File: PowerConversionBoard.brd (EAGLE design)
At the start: 152.4 x 101.6 mm, 48 parts, among them U1 LM2678, U2 LM2678

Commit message: Final touch
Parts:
- renumbered J4 to +5V_3.3V, U$8 to 5V_3.3V
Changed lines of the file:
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@@
 <attribute name="VALUE" x="143.7132" y="77.6986" size="0.6096" layer="27" font="vector" ratio="20"/>
 </element>
-<element name="J4" library="SparkFun-Connectors" library_urn="urn:adsk.eagle:library:513" package="BANANA_CONN" package3d_urn="urn:adsk.eagle:package:38018/1" value="" x="96.012" y="96.012" smashed="yes">
-<attribute name="NAME" x="93.472" y="99.314" size="0.6096" layer="25" font="vector" ratio="20"/>
+<element name="+5V_3.3V" library="SparkFun-Connectors" library_urn="urn:adsk.eagle:library:513" package="BANANA_CONN" package3d_urn="urn:adsk.eagle:package:38018/1" value="" x="96.012" y="96.012" smashed="yes">
+<attribute name="NAME" x="93.98" y="92.075" size="0.6096" layer="25" font="vector" ratio="20"/>
 <attribute name="VALUE" x="93.472" y="92.075" size="0.6096" layer="27" font="vector" ratio="20"/>
 </element>
@@
 <attribute name="NAME" x="137.5664" y="92.71" size="0.6096" layer="25"/>
 </element>
-<element name="U$8" library="TP" package="TP" value="TP" x="103.0224" y="96.393" smashed="yes">
-<attribute name="NAME" x="100.7618" y="91.3384" size="1.778" layer="25"/>
+<element name="5V_3.3V" library="TP" package="TP" value="TP" x="103.0224" y="96.393" smashed="yes">
+<attribute name="NAME" x="100.7618" y="92.8624" size="0.6096" layer="25"/>
 </element>
 <element name="U$12" library="ET60S-02-24-02-X-VP-GP" package="ET60S-02-24-02-X-VP-GP" value="ET60S-02-24-02-X-VP-GP" x="76.2" y="12.7" smashed="yes">
@@
 <contactref element="U$4" pad="P$2"/>
 <contactref element="R1" pad="2"/>
-<contactref element="J4" pad="P$1"/>
+<contactref element="+5V_3.3V" pad="P$1"/>
 <wire x1="77.6986" y1="83.5856" x2="71.3486" y2="83.5856" width="1.27" layer="1"/>
 <wire x1="84.0486" y1="83.5856" x2="77.6986" y2="83.5856" width="1.27" layer="1"/>
 <wire x1="84.0486" y1="91.5416" x2="84.0486" y2="83.5856" width="1.27" layer="1"/>
 <contactref element="U$7" pad="2"/>
-<contactref element="U$8" pad="P$1"/>
+<contactref element="5V_3.3V" pad="P$1"/>
 <wire x1="84.0486" y1="91.5416" x2="83.1986" y2="91.5416" width="1.27" layer="1"/>
 <wire x1="71.3486" y1="83.5856" x2="67.773" y2="80.01" width="1.016" layer="1"/>

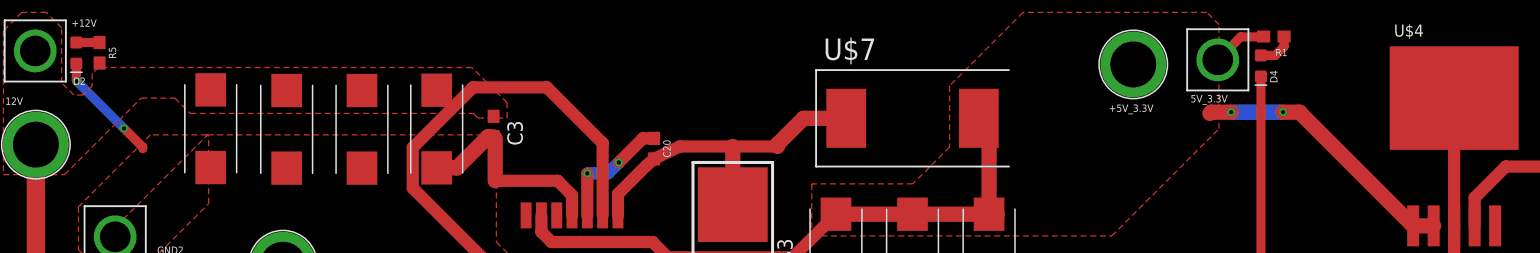
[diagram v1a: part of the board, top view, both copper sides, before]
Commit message: fixed the forward/backward annotation error
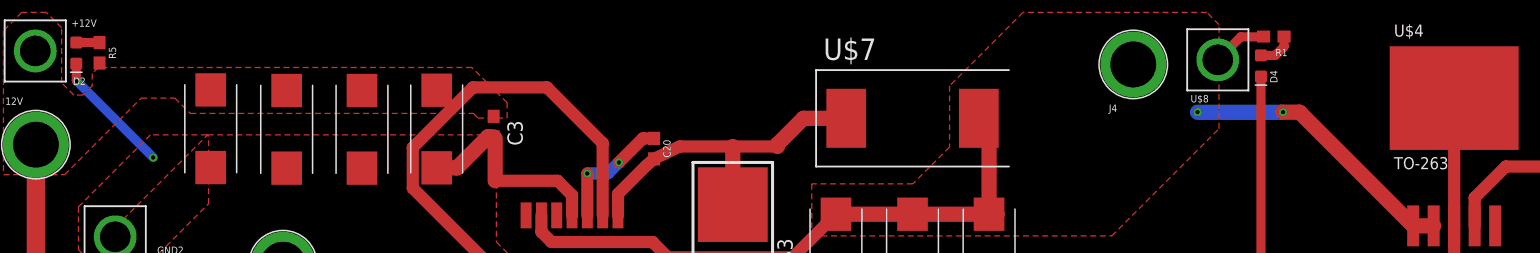
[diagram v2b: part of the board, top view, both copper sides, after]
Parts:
- renumbered +5V_3.3V to J4, 5V_3.3V to U$8
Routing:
- net GND: track 260.8 -> 261.9 mm
- net +5V_3.3V: track 77.5 -> 78.4 mm

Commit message: fixed weird
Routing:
- net +12V: track 138.4 -> 113.5 mm, vias 3 -> 2

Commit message: Board presentation file
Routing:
- net +12V: track 113.5 -> 67.4 mm, vias 2 -> 0
- net GND: track 261.9 -> 261.1 mm, vias 4 -> 5
- removed copper zone on layer 16, net +12V
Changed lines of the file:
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@@
 <?xml version="1.0" encoding="utf-8"?>
 <!DOCTYPE eagle SYSTEM "eagle.dtd">
-<eagle version="9.5.1">
+<eagle version="9.5.0">
 <drawing>
 <settings>
@@
 </class>
 </classes>
-<designrules name="ECE_Senior_Design">
+<designrules name="ECE_Senior_Design (1)">
 <description language="de">&lt;b&gt;EAGLE Design Rules&lt;/b&gt;
 &lt;p&gt;
@@
 <contactref element="U$9" pad="8"/>
 <contactref element="U$9" pad="10"/>
-<polygon width="0.254" layer="1">
-<vertex x="2.286" y="86.868"/>
-<vertex x="7.366" y="86.868"/>
-<vertex x="13.716" y="93.218"/>
-<vertex x="16.51" y="93.218"/>
-<vertex x="17.78" y="91.948"/>
-<vertex x="41.275" y="91.948"/>
-<vertex x="41.656" y="91.567"/>
-<vertex x="44.069" y="91.567"/>
-<vertex x="44.069" y="92.837"/>
-<vertex x="41.148" y="95.758"/>
-<vertex x="10.16" y="95.758"/>
-<vertex x="9.652" y="95.25"/>
-<vertex x="9.652" y="94.234"/>
-<vertex x="8.89" y="93.472"/>
-<vertex x="8.128" y="93.472"/>
-<vertex x="7.112" y="94.488"/>
-<vertex x="7.112" y="99.06"/>
-<vertex x="5.842" y="100.33"/>
-<vertex x="3.81" y="100.33"/>
-<vertex x="2.286" y="98.806"/>
-</polygon>
 <wire x1="51.9938" y1="83.4898" x2="51.9938" y2="89.4842" width="1.016" layer="1"/>
 <contactref element="U1" pad="2"/>
@@
 <wire x1="44.704" y1="53.34" x2="43.8785" y2="54.1655" width="1.016" layer="1"/>
 <wire x1="48.514" y1="52.832" x2="48.006" y2="53.34" width="1.016" layer="1"/>
-<polygon width="0.254" layer="1">
-<vertex x="17.272" y="52.578"/>
-<vertex x="17.272" y="55.88"/>
-<vertex x="18.034" y="56.642"/>
-<vertex x="38.608" y="56.642"/>
-<vertex x="41.402" y="59.436"/>
-<vertex x="42.672" y="59.436"/>
-<vertex x="43.688" y="58.42"/>
-<vertex x="43.688" y="55.626"/>
-<vertex x="44.831" y="54.483"/>
-<vertex x="44.831" y="52.197"/>
-<vertex x="44.704" y="52.07"/>
-<vertex x="17.78" y="52.07"/>
-</polygon>
-<via x="16.002" y="54.3306" extent="1-16" drill="0.35"/>
-<wire x1="16.002" y1="54.3306" x2="14.2494" y2="56.0832" width="1.524" layer="16"/>
-<wire x1="14.2494" y1="56.0832" x2="14.2494" y2="75.1586" width="1.524" layer="16"/>
-<wire x1="14.2494" y1="75.1586" x2="11.7348" y2="77.6732" width="1.524" layer="16"/>
-<wire x1="11.7348" y1="77.6732" x2="6.4262" y2="77.6732" width="1.524" layer="16"/>
-<polygon width="0.254" layer="16">
-<vertex x="1.651" y="77.8256"/>
-<vertex x="1.651" y="62.1792"/>
-<vertex x="7.2644" y="62.1792"/>
-<vertex x="7.2644" y="78.1558"/>
-<vertex x="7.3152" y="78.2066"/>
-<vertex x="2.032" y="78.2066"/>
-</polygon>
-<wire x1="16.002" y1="54.3306" x2="19.2336" y2="54.3306" width="1.524" layer="1"/>
-<wire x1="19.2336" y1="54.3306" x2="19.3294" y2="54.2348" width="1.524" layer="1"/>
 <contactref element="U$12" pad="P3-1"/>
 <contactref element="U$12" pad="P3-4"/>
@@
 <contactref element="U$12" pad="P4-6"/>
 <contactref element="U$12" pad="P4-7"/>
-<wire x1="43.8785" y1="54.1655" x2="43.8785" y2="26.5715" width="1.524" layer="1"/>
-<wire x1="43.8785" y1="26.5715" x2="54" y2="16.45" width="1.524" layer="1"/>
+<wire x1="43.8785" y1="54.1655" x2="43.8785" y2="26.5715" width="1.778" layer="1"/>
+<wire x1="54" y1="16.45" x2="43.8785" y2="26.5715" width="1.778" layer="1"/>
 <polygon width="0.254" layer="1">
 <vertex x="53.213" y="17.653"/>
@@
 <vertex x="52.324" y="16.764"/>
 </polygon>
-<wire x1="4.9784" y1="79.121" x2="6.4262" y2="77.6732" width="1.524" layer="1"/>
-<via x="6.4262" y="77.6732" extent="1-16" drill="0.35"/>
-<wire x1="4.9784" y1="89.3572" x2="4.9784" y2="79.121" width="1.524" layer="1"/>
 <wire x1="51.9938" y1="89.4842" x2="47.371" y2="94.107" width="1.016" layer="1"/>
 <wire x1="47.371" y1="94.107" x2="41.2356125" y2="94.107" width="1.016" layer="1"/>
+<polygon width="0.254" layer="1">
+<vertex x="5.969" y="100.33"/>
+<vertex x="3.556" y="100.33"/>
+<vertex x="1.651" y="98.425"/>
+<vertex x="1.651" y="62.23"/>
+<vertex x="7.239" y="62.23"/>
+<vertex x="17.653" y="51.816"/>
+<vertex x="43.815" y="51.816"/>
+<vertex x="45.085" y="53.086"/>
+<vertex x="45.085" y="57.531"/>
+<vertex x="43.053" y="59.563"/>
+<vertex x="40.64" y="59.563"/>
+<vertex x="38.1" y="57.023"/>
+<vertex x="16.256" y="57.023"/>
+<vertex x="7.239" y="66.04"/>
+<vertex x="7.239" y="85.217"/>
+<vertex x="13.97" y="91.948"/>
+<vertex x="41.402" y="91.948"/>
+<vertex x="42.164" y="91.186"/>
+<vertex x="44.069" y="91.186"/>
+<vertex x="44.45" y="91.567"/>
+<vertex x="44.45" y="94.107"/>
+<vertex x="42.418" y="96.139"/>
+<vertex x="11.43" y="96.139"/>
+<vertex x="11.049" y="96.52"/>
+<vertex x="9.906" y="96.52"/>
+<vertex x="9.525" y="96.139"/>
+<vertex x="9.525" y="94.234"/>
+<vertex x="8.89" y="93.599"/>
+<vertex x="8.001" y="93.599"/>
+<vertex x="7.112" y="94.488"/>
+<vertex x="7.112" y="99.187"/>
+</polygon>
 </signal>
 <signal name="GND">
@@
 <wire x1="49.4538" y1="85.1662" x2="49.4538" y2="83.4898" width="1.016" layer="1"/>
 <wire x1="48.26" y1="86.36" x2="49.4538" y2="85.1662" width="1.016" layer="1"/>
-<wire x1="19.3294" y1="60.6748" x2="11.1956" y2="60.6748" width="1.524" layer="1"/>
-<wire x1="10.2108" y1="59.69" x2="5.715" y2="59.69" width="1.524" layer="1"/>
-<wire x1="11.1956" y1="60.6748" x2="10.2108" y2="59.69" width="1.524" layer="1"/>
-<polygon width="0.254" layer="1">
-<vertex x="1.6764" y="45.7454"/>
-<vertex x="7.239" y="45.7454"/>
-<vertex x="7.239" y="61.0616"/>
-<vertex x="1.6764" y="61.0616"/>
-</polygon>
 <polygon width="0.1524" layer="1">
 <vertex x="143.891" y="66.04"/>
@@
 <wire x1="8.3312" y1="94.6658" x2="8.3312" y2="96.0748" width="0.762" layer="1"/>
 <wire x1="123.952" y1="51.435" x2="119.126" y2="56.261" width="1.778" layer="16"/>
+<polygon width="0.1524" layer="16">
+<vertex x="1.651" y="60.96"/>
+<vertex x="1.651" y="45.72"/>
+<vertex x="7.239" y="45.72"/>
+<vertex x="7.239" y="60.96"/>
+</polygon>
+<wire x1="19.3294" y1="60.6748" x2="15.2088" y2="60.6748" width="1.524" layer="1"/>
+<wire x1="15.2088" y1="60.6748" x2="15.113" y2="60.579" width="1.524" layer="1"/>
+<via x="15.113" y="60.579" extent="1-16" drill="0.35"/>
+<wire x1="15.113" y1="60.579" x2="12.954" y2="58.42" width="1.524" layer="16"/>
+<wire x1="12.954" y1="58.42" x2="7.112" y2="58.42" width="1.524" layer="16"/>
 </signal>
 <signal name="+5V">
@@
 <wire x1="146.5834" y1="30.6188" x2="146.5208" y2="30.5562" width="1.016" layer="1"/>
 <wire x1="146.5834" y1="34.9758" x2="146.5834" y2="30.6188" width="0.762" layer="1"/>
-<polygon width="0.254" layer="16" isolate="0.8128">
-<vertex x="66.04" y="16.2814"/>
-<vertex x="66.04" y="9.398"/>
-<vertex x="67.437" y="8.001"/>
-<vertex x="74.93" y="8.001"/>
-<vertex x="74.93" y="12.827"/>
-<vertex x="71.4756" y="16.2814"/>
+<polygon width="0.254" layer="16">
+<vertex x="66.929" y="16.383"/>
+<vertex x="66.04" y="15.494"/>
+<vertex x="66.04" y="8.89"/>
+<vertex x="66.421" y="8.509"/>
+<vertex x="75.565" y="8.509"/>
+<vertex x="76.2" y="9.144"/>
+<vertex x="76.2" y="12.446"/>
+<vertex x="72.39" y="12.446"/>
+<vertex x="72.39" y="16.383"/>
 </polygon>
 </signal>
@@
 <polygon width="0.1524" layer="16">
 <vertex x="143.891" y="76.2"/>
-<vertex x="143.891" y="67.183"/>
-<vertex x="149.479" y="67.183"/>
+<vertex x="143.891" y="67.31"/>
+<vertex x="149.479" y="67.31"/>
 <vertex x="149.479" y="76.2"/>
 </polygon>
@@
 <mfgpreviewcolor name="substratecolor" color="0xFF786E46"/>
 </mfgpreviewcolors>
-<errors>
-</errors>
 </board>
 </drawing>
